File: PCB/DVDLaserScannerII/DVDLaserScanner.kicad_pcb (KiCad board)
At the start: 2 copper layers, 144 x 80 mm, 83 parts, among them Q1 Q_NMOS_GDS, SW1 BUT, U1 MCP4922-E/SL, U10 Con45, U11 Con45, U13 TLC2274, U2 MCP4922-E/SL, U3 ARDUINO_MICRO, U4 TCA0372_DWG, U5 TCA0372_DWG, U6 TCA0372_DWG, U7 MCP6002, U8 MCP4922-E/SL, U9 TLC2274, X1 MountPad3, X2 MountPad3, X3 MountPad3, X4 MountPad3, X5 PAD, X6 PAD, X7 PAD

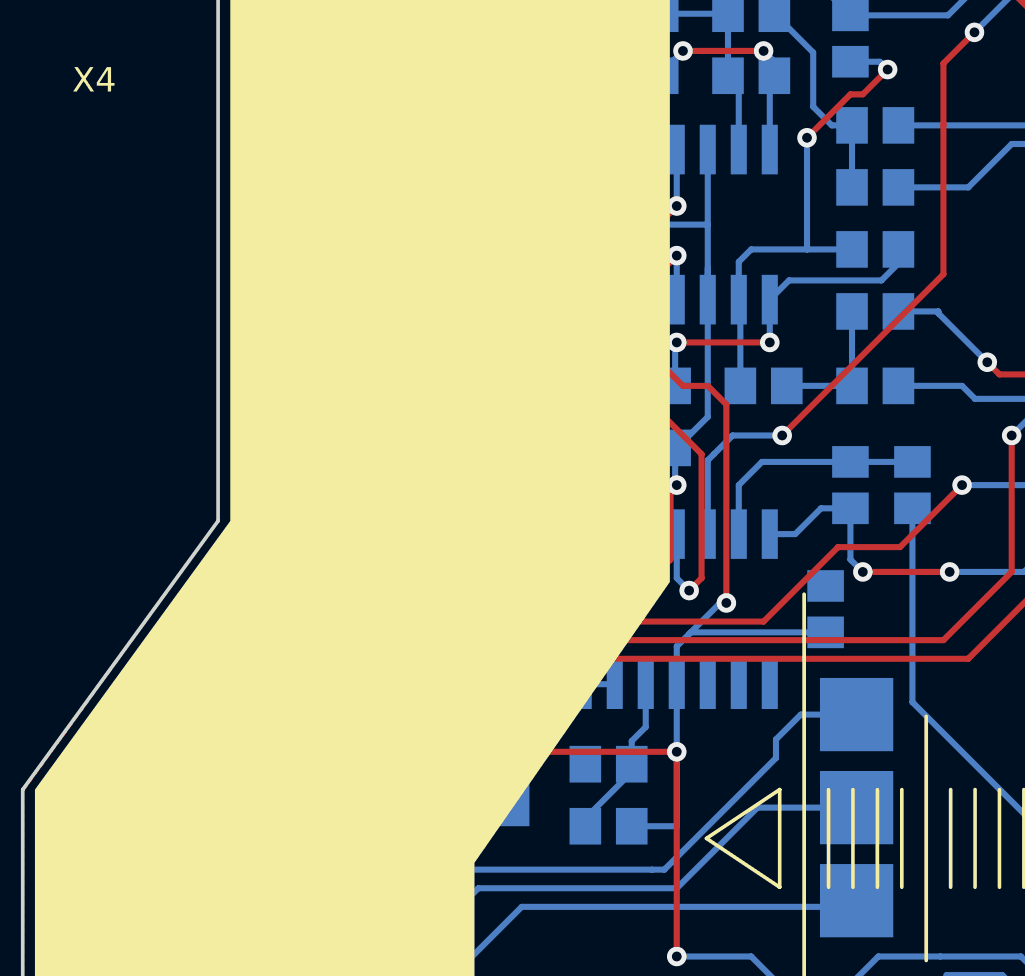
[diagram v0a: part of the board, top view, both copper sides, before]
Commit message: Finally fixed error on U9 / U13 and updated BOM
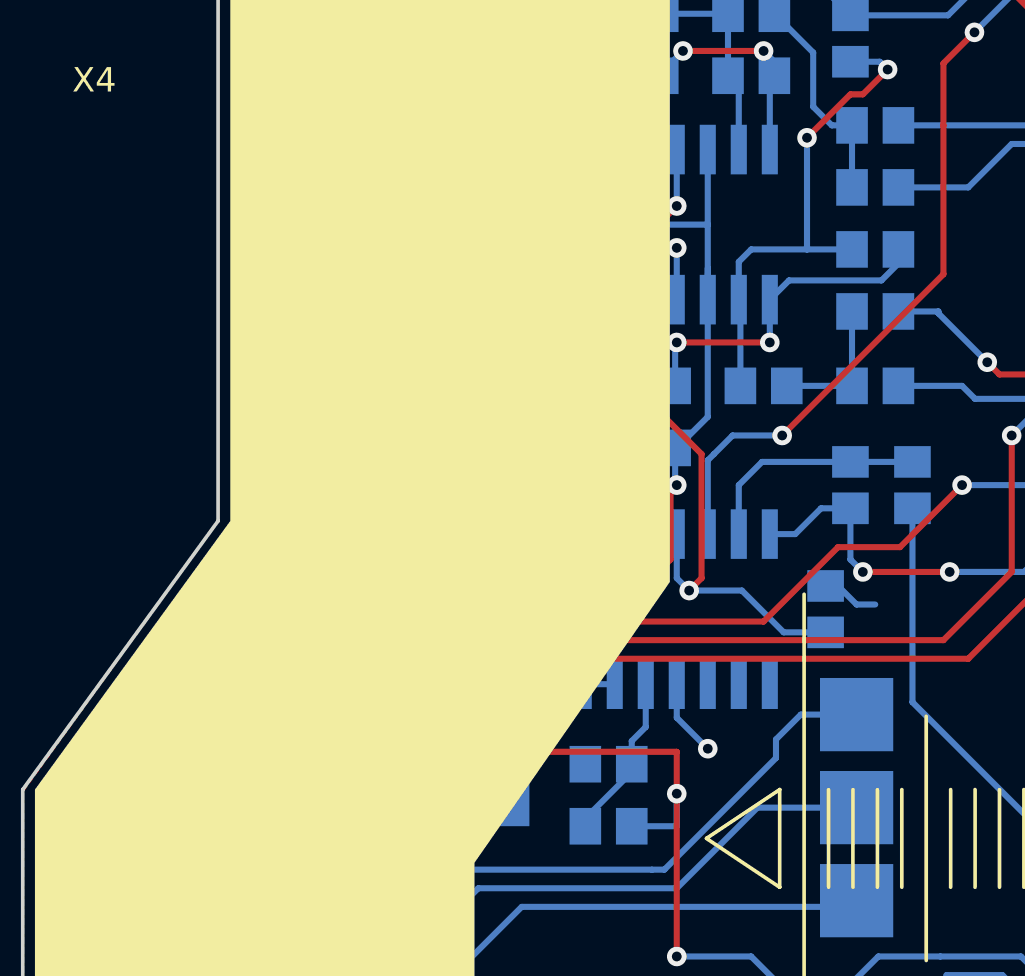
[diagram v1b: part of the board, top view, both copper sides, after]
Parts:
- C12: value CP_Small -> 100nF
- R2, R4: value 56k -> 270k
- R34: value 4.7k -> 560k
- R35: value 4.7k -> 2.7k
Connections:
- U13 pad 11: VCC_BLUE -> GND
- U13 pad 4: GND -> VCC_BLUE
- U9 pad 11: VCC_BLUE -> GND
- U9 pad 4: GND -> VCC_BLUE
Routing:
- net VCC_BLUE: track 498.1 -> 524.7 mm
- net GND: track 358.8 -> 343.6 mm
